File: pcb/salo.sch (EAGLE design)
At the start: 12 parts, among them IC2 LT1763CS8-3.3

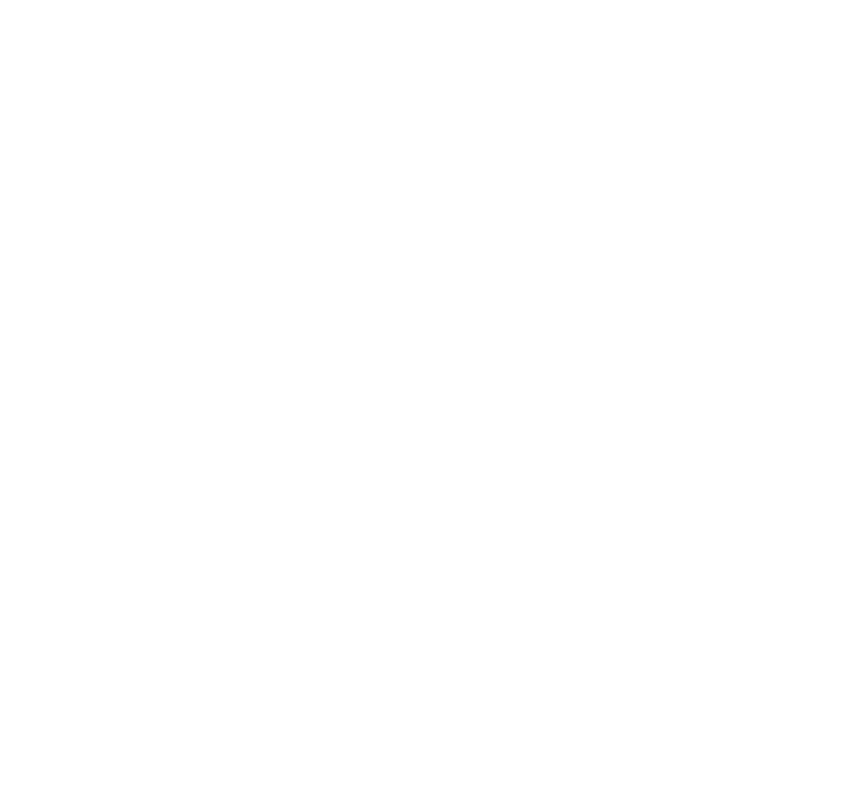
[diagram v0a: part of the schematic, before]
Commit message: Add 2x N-channel enhancement MOSFET, SO-8.
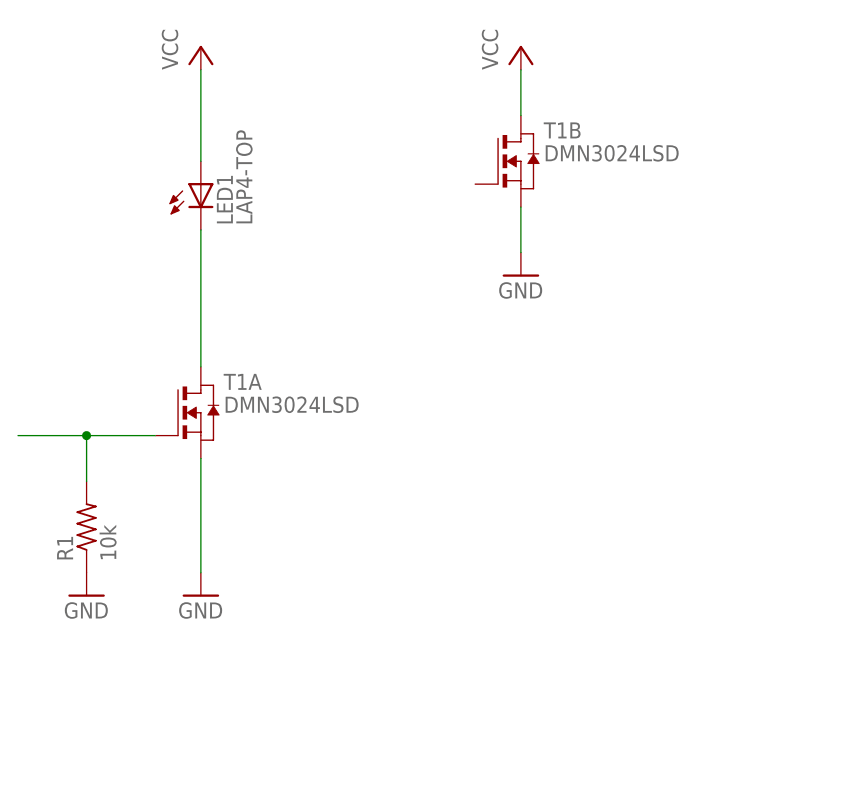
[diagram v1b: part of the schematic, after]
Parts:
- added LED1: LAP4-TOP, led:LAP4-TOP
- added R1: 10k, rcl:R-US_R0805
- added T1: DMN3024LSD, zetex:DMN3024LSD
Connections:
- new net N$2: R1.2, T1A.G
- new net N$3: LED1.C, T1A.D
- net GND: now also R1.1, T1A.S, T1B.S
- net VCC: now also LED1.A, T1B.D
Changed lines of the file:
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@@
 <part name="+3V4" library="supply1" deviceset="+3V3" device=""/>
 <part name="+3V5" library="supply1" deviceset="+3V3" device=""/>
+<part name="P+2" library="supply1" deviceset="VCC" device=""/>
+<part name="GND2" library="supply1" deviceset="GND" device=""/>
+<part name="T1" library="zetex" deviceset="DMN3024LSD" device=""/>
+<part name="P+3" library="supply1" deviceset="VCC" device=""/>
+<part name="GND6" library="supply1" deviceset="GND" device=""/>
+<part name="GND7" library="supply1" deviceset="GND" device=""/>
+<part name="R1" library="rcl" deviceset="R-US_" device="R0805" value="10k"/>
+<part name="LED1" library="led" deviceset="*P4" device="-TOP" technology="LA"/>
 </parts>
 <sheets>
@@
 <instance part="+3V4" gate="G$1" x="203.2" y="162.56"/>
 <instance part="+3V5" gate="G$1" x="208.28" y="162.56"/>
+<instance part="P+2" gate="VCC" x="45.72" y="165.1"/>
+<instance part="GND2" gate="1" x="45.72" y="104.14"/>
+<instance part="T1" gate="A" x="45.72" y="124.46"/>
+<instance part="T1" gate="B" x="81.28" y="152.4"/>
+<instance part="P+3" gate="VCC" x="81.28" y="165.1"/>
+<instance part="GND6" gate="1" x="81.28" y="139.7"/>
+<instance part="GND7" gate="1" x="33.02" y="104.14"/>
+<instance part="R1" gate="G$1" x="33.02" y="111.76" rot="R90"/>
+<instance part="LED1" gate="G$1" x="45.72" y="149.86"/>
 </instances>
 <busses>
@@
 <wire x1="246.38" y1="127" x2="228.6" y2="127" width="0.1524" layer="91"/>
 <label x="228.6" y="127" size="1.778" layer="95"/>
+</segment>
+<segment>
+<pinref part="T1" gate="A" pin="S"/>
+<pinref part="GND2" gate="1" pin="GND"/>
+<wire x1="45.72" y1="119.38" x2="45.72" y2="106.68" width="0.1524" layer="91"/>
+</segment>
+<segment>
+<pinref part="T1" gate="B" pin="S"/>
+<pinref part="GND6" gate="1" pin="GND"/>
+<wire x1="81.28" y1="147.32" x2="81.28" y2="142.24" width="0.1524" layer="91"/>
+</segment>
+<segment>
+<pinref part="GND7" gate="1" pin="GND"/>
+<pinref part="R1" gate="G$1" pin="1"/>
 </segment>
 </net>
@@
 <wire x1="246.38" y1="124.46" x2="228.6" y2="124.46" width="0.1524" layer="91"/>
 <label x="228.6" y="124.46" size="1.778" layer="95"/>
+</segment>
+<segment>
+<pinref part="P+3" gate="VCC" pin="VCC"/>
+<pinref part="T1" gate="B" pin="D"/>
+<wire x1="81.28" y1="162.56" x2="81.28" y2="157.48" width="0.1524" layer="91"/>
+</segment>
+<segment>
+<pinref part="P+2" gate="VCC" pin="VCC"/>
+<pinref part="LED1" gate="G$1" pin="A"/>
+<wire x1="45.72" y1="162.56" x2="45.72" y2="152.4" width="0.1524" layer="91"/>
 </segment>
 </net>
@@
 </segment>
 </net>
+<net name="N$2" class="0">
+<segment>
+<pinref part="R1" gate="G$1" pin="2"/>
+<wire x1="33.02" y1="116.84" x2="33.02" y2="121.92" width="0.1524" layer="91"/>
+<pinref part="T1" gate="A" pin="G"/>
+<wire x1="33.02" y1="121.92" x2="40.64" y2="121.92" width="0.1524" layer="91"/>
+<wire x1="33.02" y1="121.92" x2="25.4" y2="121.92" width="0.1524" layer="91"/>
+<junction x="33.02" y="121.92"/>
+</segment>
+</net>
+<net name="N$3" class="0">
+<segment>
+<pinref part="LED1" gate="G$1" pin="C"/>
+<pinref part="T1" gate="A" pin="D"/>
+<wire x1="45.72" y1="144.78" x2="45.72" y2="129.54" width="0.1524" layer="91"/>
+</segment>
+</net>
